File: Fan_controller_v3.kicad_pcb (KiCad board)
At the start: 4 copper layers, 52 parts, among them J1 Load2, J2 Dig_mod_iface, K1 HFD2_005-S-L2-D_Split, K2 HFD2_005-S-L2-D_Split, Q1 2N5551S, Q2 2N5551S, Q3 BSS138, Q4 BSS138, Q5 2N5551S, Q6 2N5551S, U1 ADuM1251ARZ, U2 PCA9536DP

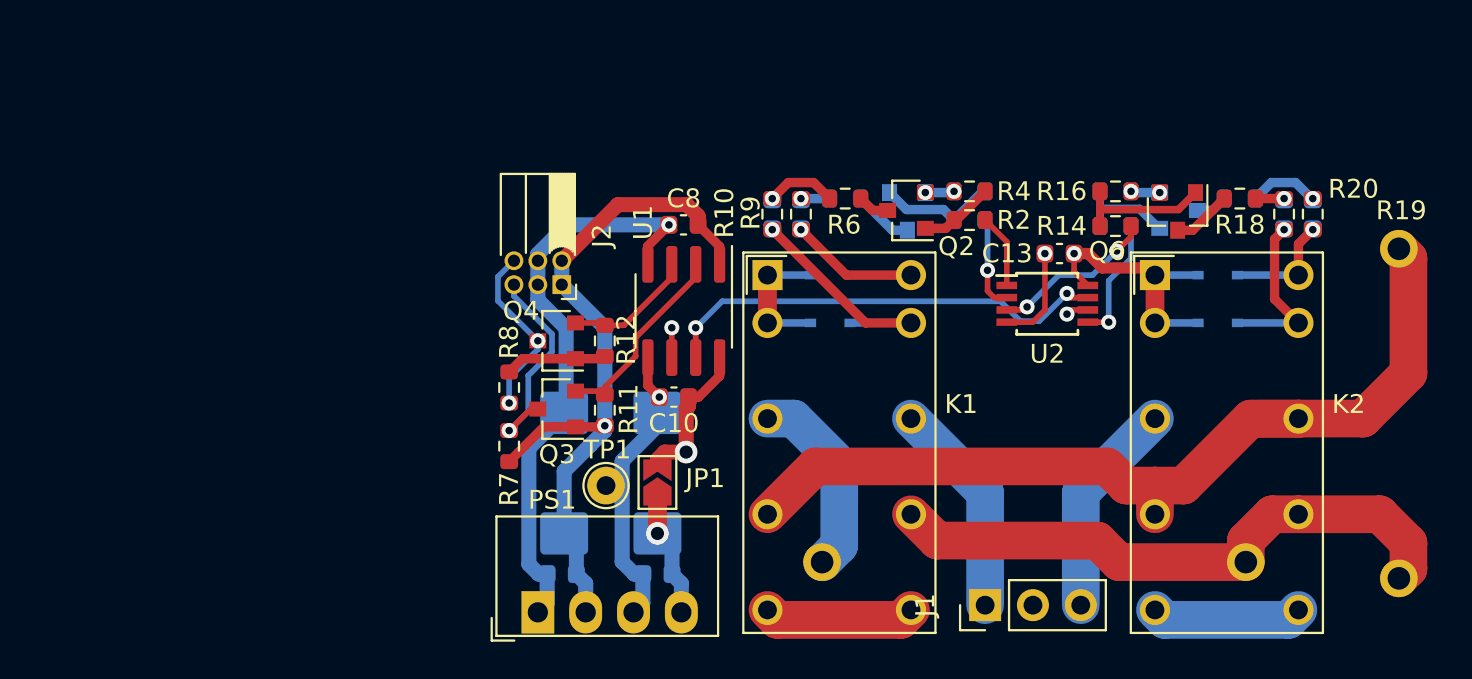
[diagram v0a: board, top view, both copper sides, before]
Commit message: Сформирован перечень элементов, 3D-модель, исправлены ошибки, реализована панелизация платы.
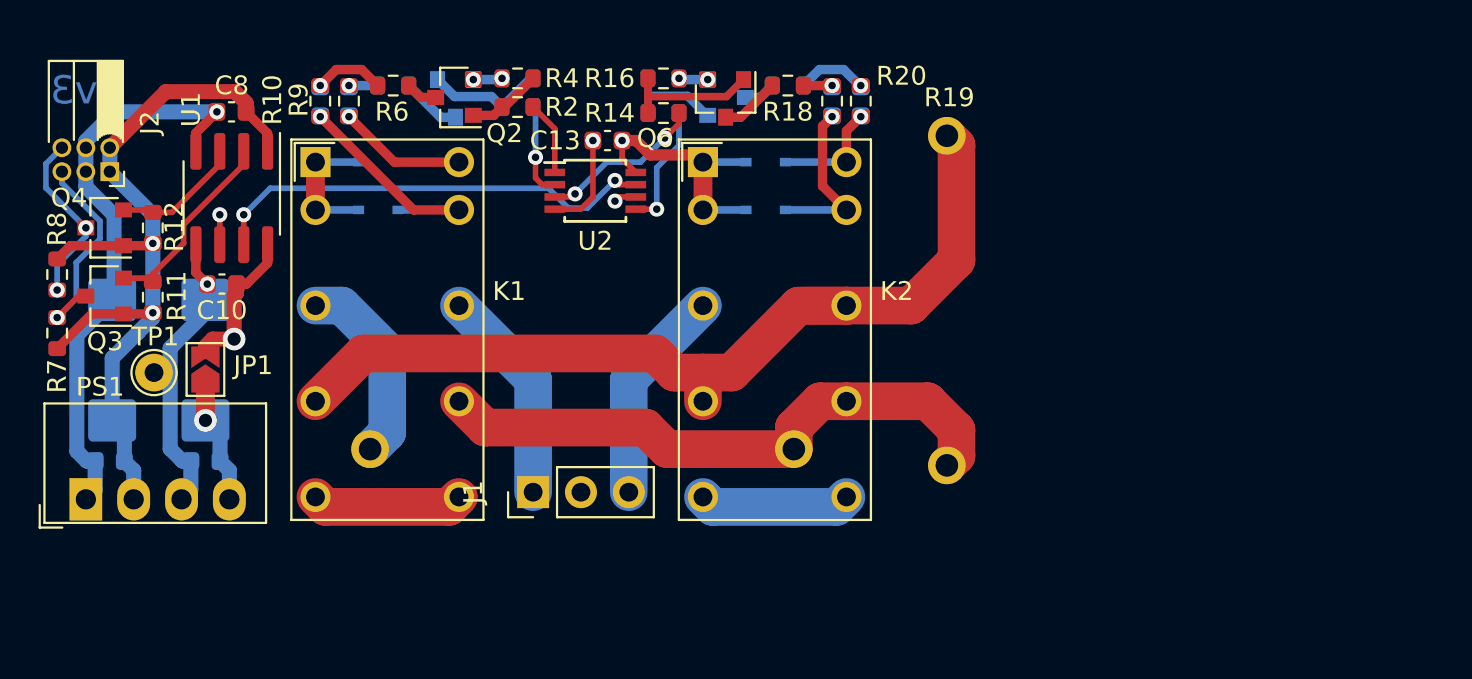
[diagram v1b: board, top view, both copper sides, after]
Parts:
- moved C1 24.7 mm to (58.4, 72.0)
- moved C10 24.7 mm to (64.2, 67.9)
- moved C13 24.7 mm to (84.7, 60.3)
- moved C2 24.7 mm to (58.3, 77.3)
- moved C5 24.7 mm to (72.1, 76.7)
- moved C7 24.7 mm to (102.7, 60.0)
- moved C8 24.7 mm to (64.8, 58.8)
- moved D2 24.7 mm to (72.5, 64.0)
- moved D4 24.7 mm to (93.1, 64.0)
- moved J1 24.7 mm to (80.8, 79.0)
- moved J2 24.7 mm to (58.3, 62.0)
- moved PS1 24.7 mm to (57.0, 79.3)
- moved Q1 24.7 mm to (76.6, 58.1)
- moved Q3 24.7 mm to (58.0, 68.6)
- moved Q4 24.7 mm to (58.0, 64.9)
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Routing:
- net +5P: vias 1 -> 2
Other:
- board text added: "v3"

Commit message: Последние изменения в BOM
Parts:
- added REF**: MountingHole_2.29x5.46mm, Modules:MountingHole_2.29x5.46mm, F.Cu at (103.1, 59.4)
- added REF**: MountingHole_2.29x3.81mm, Modules:MountingHole_2.29x3.81mm, F.Cu at (100.3, 65.5)
- added REF**: MountingHole_2.29x3.81mm, Modules:MountingHole_2.29x3.81mm, F.Cu at (92.7, 65.5)
- added REF**: MountingHole_2.29x3.81mm, Modules:MountingHole_2.29x3.81mm, F.Cu at (79.7, 65.5)
- added REF**: MountingHole_2.29x3.81mm, Modules:MountingHole_2.29x3.81mm, F.Cu at (72.2, 65.5)
- added REF**: MountingHole_D2.0mm, Modules:MountingHole_D2.0mm, F.Cu at (69.7, 67.9)
- added REF**: MountingHole_D2.0mm, Modules:MountingHole_D2.0mm, F.Cu at (69.7, 73.1)
- added REF**: MountingHole_D2.0mm, Modules:MountingHole_D2.0mm, F.Cu at (69.8, 78.3)
- moved C10 3.07 mm to (67.1, 66.9)
- moved C11 3.07 mm to (101.1, 57.2)
- moved C12 3.07 mm to (99.5, 57.2)
- moved C13 3.07 mm to (87.6, 59.3)
- moved C2 3.07 mm to (61.2, 76.3)
- moved C3 3.07 mm to (73.9, 57.2)
- moved C4 3.07 mm to (72.4, 57.2)
- moved C5 3.07 mm to (75.0, 75.7)
- moved C7 3.07 mm to (105.6, 59.0)
- moved C8 3.07 mm to (67.7, 57.8)
- moved J1 3.07 mm to (83.7, 78.0)
- moved J2 3.07 mm to (61.2, 61.0)
- moved K1 3.07 mm to (72.1, 60.4)
- moved Q1 3.07 mm to (79.5, 57.1)
- moved Q2 3.07 mm to (79.5, 57.0)
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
